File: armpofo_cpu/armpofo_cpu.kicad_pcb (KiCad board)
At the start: 2 copper layers, 82 parts, among them J1 USB_OTG, J2 Conn_01x01, J3 Conn_01x01, J4 Conn_01x16, J5 Conn_01x20, J6 Conn_02x16_Odd_Even, J7 Conn_01x08, J8 Micro_SD_Card, Q1 Q_PMOS_GDS, Q2 Q_PMOS_GDS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

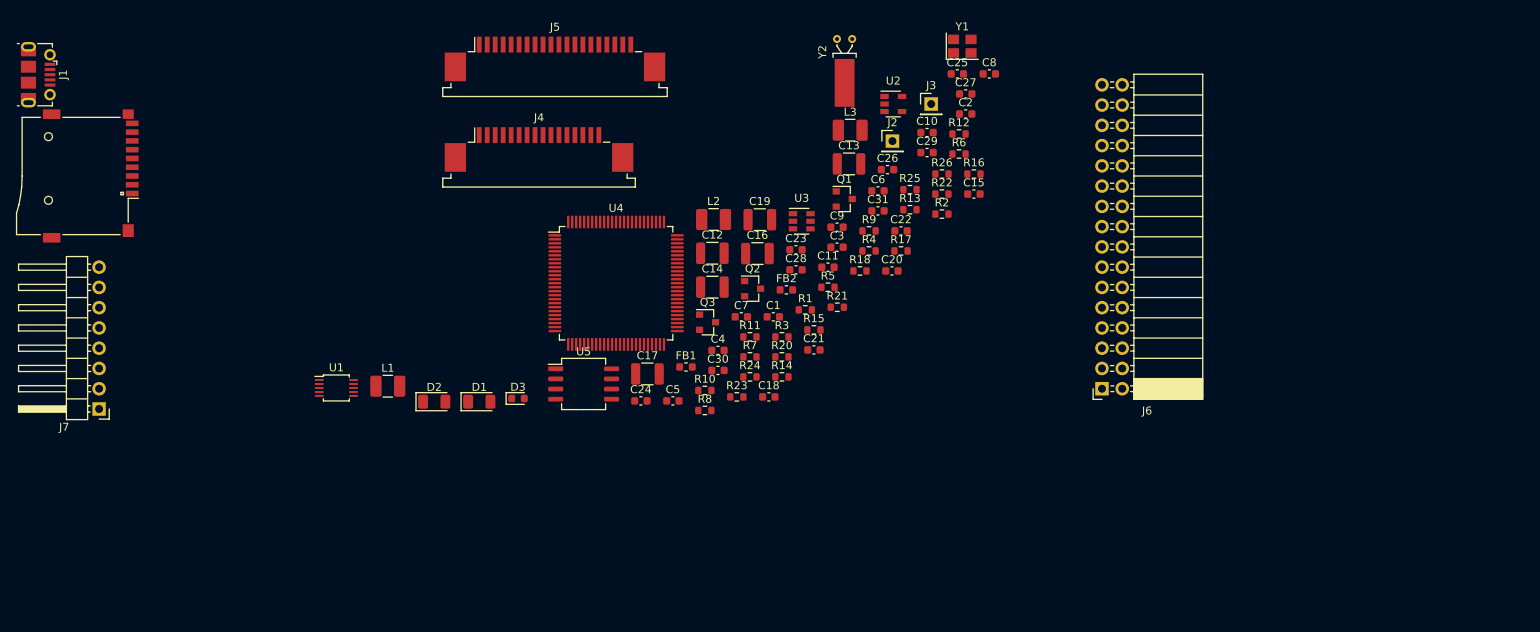
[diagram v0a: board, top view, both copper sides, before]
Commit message: - CPU board finalisch edge cuts - Keyboard mounting modified to 2.2 mm holes
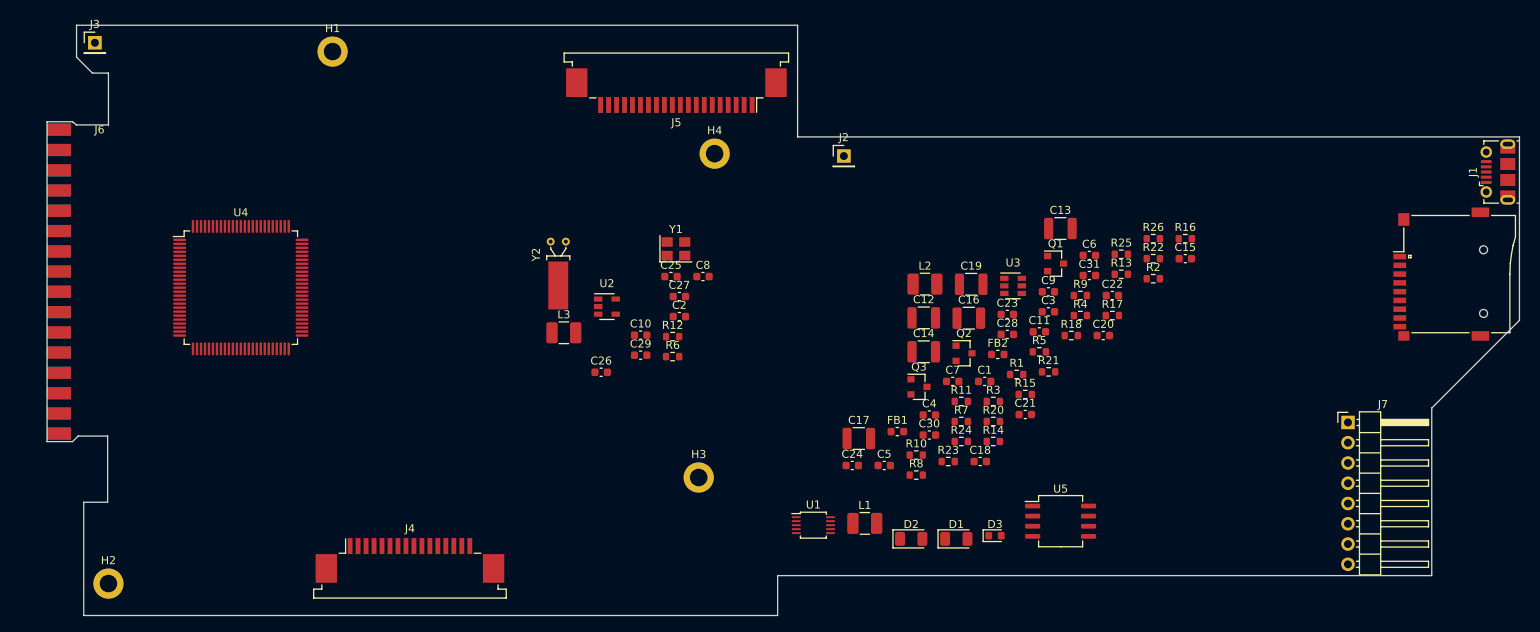
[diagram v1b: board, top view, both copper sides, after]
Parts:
- added H1: 2mm, MountingHole:MountingHole_2.2mm_M2_DIN965_Pad, F.Cu at (104.2, 73.3)
- added H2: 2mm, MountingHole:MountingHole_2.2mm_M2_DIN965_Pad, F.Cu at (76.1, 140.0)
- added H3: 2mm, MountingHole:MountingHole_2.2mm_M2_DIN965_Pad, F.Cu at (150.1, 126.7)
- added H4: 2mm, MountingHole:MountingHole_2.2mm_M2_DIN965_Pad, F.Cu at (152.1, 86.1)
- J6: footprint Connector_PinSocket_2.54mm:PinSocket_2x16_P2.54mm_Horizontal -> PROJECT_LOCAL:Conn_Edge_PinSocket_2x16_2.54mm
- moved J1 183.4 mm to (250.3, 88.4), turned to 90 degrees
- moved J8 180.3 mm to (248.5, 101.2), turned to 90 degrees
- moved J7 156.6 mm to (231.5, 119.8), turned to 0 degrees
- moved J6 134.7 mm to (69.9, 83.1), turned to 0 degrees
- moved J3 105.1 mm to (74.4, 72.2)
- moved L1 62.2 mm to (170.9, 132.5)
- moved D1 62.2 mm to (182.4, 134.4)
- moved D2 62.2 mm to (176.7, 134.4)
- moved D3 62.2 mm to (187.2, 134.0)
- moved U1 62.2 mm to (164.5, 132.7)
- moved U5 62.2 mm to (195.5, 132.2)
- moved J4 54.0 mm to (113.9, 137.1)
- moved U4 47.0 mm to (92.7, 102.9)
- moved C10 44.0 mm to (142.8, 108.9)
- moved C29 44.0 mm to (142.8, 111.4)
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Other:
- board outline added: 184.6 x 74 mm
- board text added: "Keyboard Connector"
- board text added: "LCD Connector"

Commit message: final form
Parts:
- moved J2 5.11 mm to (164.4, 89.7)
- moved J8 3.83 mm to (249.5, 104.9)
- moved J1 2.75 mm to (250.8, 91.1)
- moved J7 1.58 mm to (232.0, 121.3)
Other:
- board size 184.6 x 74 mm -> 185.1 x 74 mm

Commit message: some progress
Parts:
- added C32: 1nF, Capacitor_SMD:C_0603_1608Metric, F.Cu at (202.7, 117.8)
- added D4: SS24, Diode_SMD:D_1206_3216Metric, F.Cu at (214.4, 111.9)
- added J9: Conn_01x01, Connector_PinHeader_2.54mm:PinHeader_1x01_P2.54mm_Vertical, F.Cu at (80.7, 72.5)
- added R19: 100k, Resistor_SMD:R_0603_1608Metric, F.Cu at (145.1, 111.1)
- added R27: 100k, Resistor_SMD:R_0603_1608Metric, F.Cu at (145.1, 114.5)
- added R28: 22R, Resistor_SMD:R_0603_1608Metric, F.Cu at (245.5, 92.1)
- added R29: 22R, Resistor_SMD:R_0603_1608Metric, F.Cu at (245.5, 94.6)
- U1: footprint Package_SO:TSSOP-10_3x3mm_P0.5mm -> PROJECT_LOCAL:DLA0010A
- moved R26 110.7 mm to (96.6, 102.8)
- moved C31 106.3 mm to (92.8, 102.8)
- moved R16 103.4 mm to (112.9, 129.2)
- moved U5 102.1 mm to (96.2, 108.4)
- moved C6 95.3 mm to (105.5, 116.7)
- moved C3 89.3 mm to (104.7, 107.3)
- moved C1 82.4 mm to (104.7, 100.7)
- moved R1 79.8 mm to (114.4, 88.3)
- moved L3 78.4 mm to (211.1, 117.0)
- moved C7 76.7 mm to (105.5, 120.0)
- moved R5 76.1 mm to (119.9, 89.0)
- moved C4 74.5 mm to (105.0, 110.6)
- moved C22 71.3 mm to (130.6, 105.1)
- moved C5 69.4 mm to (105.0, 113.7)
- moved C25 66.5 mm to (208.9, 124.9)
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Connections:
- net /5V-INPUT renamed /3-5V
- J1 pad 2: /USB-DM -> Net-(J1-Pad2)
- J1 pad 3: /USB-DP -> Net-(J1-Pad3)
- U4 pad 15: /LED1 -> /ADC-5V
- U4 pad 62: Net-(U4-Pad62) -> /LED1
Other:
- board text added: "BAT+"
- board text added: "BAT-"

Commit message: routing progress 70%
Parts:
- removed C27: 100nF, Capacitor_SMD:C_0603_1608Metric
- removed R8: 0R, Resistor_SMD:R_0603_1608Metric
- added C33: 100nF, Capacitor_SMD:C_0603_1608Metric, F.Cu at (208.0, 92.0)
- added J10: Conn_01x16, Connector_PinHeader_1.27mm:PinHeader_1x16_P1.27mm_Vertical, F.Cu at (106.2, 142.9)
- added J11: Conn_01x20, Connector_PinHeader_1.27mm:PinHeader_1x20_P1.27mm_Vertical, F.Cu at (135.4, 71.1)
- J4: moved to B.Cu
- R10: footprint Resistor_SMD:R_0603_1608Metric -> Resistor_SMD:R_1206_3216Metric
- R4: value 0R -> 1k
- U1: value TPS63802 -> TPS63030DSK; footprint PROJECT_LOCAL:DLA0010A -> Package_SON:WSON-10-1EP_2.5x2.5mm_P0.5mm_EP1.2x2mm
- moved R4 69.3 mm to (149.4, 103.1), turned to 180 degrees
- moved C32 58.3 mm to (146.3, 103.1), turned to 180 degrees
- moved C25 45.6 mm to (176.5, 92.8), turned to 270 degrees
- moved U3 44.6 mm to (171.8, 91.8), turned to 180 degrees
- moved L3 43.7 mm to (178.0, 88.5), turned to 180 degrees
- moved C24 41.2 mm to (167.8, 95.2), turned to 180 degrees
- moved R10 41.1 mm to (171.8, 88.2)
- moved D4 39.9 mm to (179.2, 93.0), turned to 270 degrees
- moved R5 38.6 mm to (136.4, 124.0), turned to 270 degrees
- moved R1 38.6 mm to (146.8, 109.2)
- moved C10 38.6 mm to (143.5, 109.2), turned to 180 degrees
- moved R12 31.7 mm to (167.0, 92.8), turned to 270 degrees
- moved Q1 28.8 mm to (182.8, 91.0), turned to 270 degrees
- moved R11 28.3 mm to (168.8, 92.8), turned to 90 degrees
- moved C1 27.6 mm to (129.3, 113.2)
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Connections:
- net Net-(J5-Pad12) renamed /LCD-CTRPWM
- C32 pad 1: Net-(C25-Pad1) -> /I-CHARGE
- C32 pad 2: /BAT+ -> GND
- D3 pad 1: /LED1 -> Net-(D3-Pad1)
- D3 pad 2: Net-(D3-Pad2) -> +3V3
- H1 pad 1: Earth_Protective -> Net-(H1-Pad1)
- H2 pad 1: Earth_Protective -> Net-(H2-Pad1)
- H3 pad 1: Earth_Protective -> Net-(H3-Pad1)
- H4 pad 1: Earth_Protective -> Net-(H4-Pad1)
- R25 pad 1: Net-(D3-Pad2) -> /LED1
- R25 pad 2: +3V3 -> Net-(D3-Pad1)
- R4 pad 1: /3-5V -> Net-(R4-Pad1)
- R4 pad 2: Net-(R4-Pad2) -> /I-CHARGE
- U1 pad 1: /3-5V -> /5VINT
- U1 pad 10: /3-5V -> Net-(R3-Pad2)
- U1 pad 2: Net-(R4-Pad2) -> Net-(L1-Pad2)
- U1 pad 4: Net-(R3-Pad2) -> Net-(L1-Pad1)
- U1 pad 5: Net-(U1-Pad5) -> /3-5V
- U1 pad 6: /5VINT -> Net-(C33-Pad1)
- U1 pad 7: Net-(L1-Pad2) -> Net-(C33-Pad1)
- U1 pad 8: GND -> Net-(C33-Pad1)
- U1 pad 9: Net-(L1-Pad1) -> GND
- U3 pad 1: /I-CHARGE -> Net-(R4-Pad1)
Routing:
- net +3V3: track 0.00 -> 240.6 mm, vias 0 -> 22
- net /BOOT0: track 0.00 -> 125.4 mm, vias 0 -> 2
- net GND: track 0.00 -> 112.4 mm, vias 0 -> 43
- net /USB5V: track 0.00 -> 108.0 mm
- net /5VINT: track 0.00 -> 107.0 mm, vias 0 -> 5
- net /TRACE-RX: track 0.00 -> 98.7 mm
- net /TRACE-TX: track 0.00 -> 98.5 mm
- net /SWDIO: track 0.00 -> 98.4 mm
- net /RESET: track 0.00 -> 95.8 mm
- net /CHARGE-PWM: track 0.00 -> 86.6 mm, vias 0 -> 2
- net /SDCARD-D2: track 0.00 -> 84.1 mm
- net /SDCARD-D3: track 0.00 -> 84.1 mm
- net /SOUND-LATCH: track 0.00 -> 83.9 mm, vias 0 -> 4
- net /SWDC: track 0.00 -> 82.7 mm
- net /SDCARD-CMD: track 0.00 -> 81.4 mm
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- added copper zone on F.Cu, net /3-5V
- added copper zone on F.Cu, net /5VINT
- added copper zone on B.Cu, net GND
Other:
- net class Default: trace_width 0.25 -> 0.2; via_dia 0.8 -> 0.6; via_drill 0.4 -> 0.3
- rule trace_min: 0.2 -> 0.156
- rule via_min_size: 0.4 -> 0.6
- board text added: "1"
- board text added: "16"
- board text added: "20"
- board text added: "5V"
- board text added: "GND"

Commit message: routing finished.
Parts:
- moved R5 18.3 mm to (119.7, 131.5), turned to 90 degrees
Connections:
- J6 pad 10: /PB6 -> /PA2
- J6 pad 11: /PA2 -> /PA5
- J6 pad 12: /PB7 -> /PA4
- J6 pad 13: /PA3 -> /PA7
- J6 pad 14: /PB11 -> /PA6
- J6 pad 15: /PA4 -> /PB5
- J6 pad 16: /PB12 -> /PA8
- J6 pad 17: /PA5 -> /PB7
- J6 pad 18: /PB13 -> /PB6
- J6 pad 19: /PA6 -> /PB12
- J6 pad 20: /PB14 -> /PB11
- J6 pad 21: /PA7 -> /PB14
- J6 pad 22: /PB15 -> /PB13
- J6 pad 23: /PA8 -> /PC1
- J6 pad 24: /PC1 -> /PB15
- J6 pad 25: /PD0 -> /PC5
- J6 pad 28: /PC5 -> /PD0
- J6 pad 7: /PA0 -> /PA1
- J6 pad 8: /PB5 -> /PA0
- J6 pad 9: /PA1 -> /PA3
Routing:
- net +3V3: track 240.6 -> 433.5 mm, vias 22 -> 29
- net /USB-DM: track 22.6 -> 152.7 mm, vias 2 -> 4
- net /USB-DP: track 24.8 -> 154.0 mm, vias 2 -> 4
- net /5VINT: track 107.0 -> 183.9 mm, vias 5 -> 10
- net /LED1: track 70.1 -> 136.5 mm, vias 0 -> 4
- net /SDCARD-D2: track 84.1 -> 149.3 mm, vias 0 -> 4
- net /SDCARD-D1: track 75.5 -> 139.1 mm, vias 0 -> 4
- net /SDCARD-D3: track 84.1 -> 145.4 mm, vias 0 -> 4
- net /SDCARD-D0: track 80.4 -> 139.6 mm, vias 0 -> 4
- net /SDCARD-CK: track 80.7 -> 139.0 mm, vias 0 -> 2
- net /PA0: track 13.0 -> 69.5 mm, vias 0 -> 5
- net /SDCARD-CMD: track 81.4 -> 137.6 mm, vias 0 -> 2
- net /PA1: track 13.0 -> 66.2 mm, vias 0 -> 4
- net /PA2: track 12.9 -> 65.1 mm, vias 0 -> 5
- net /PA3: track 12.7 -> 61.9 mm, vias 0 -> 4
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
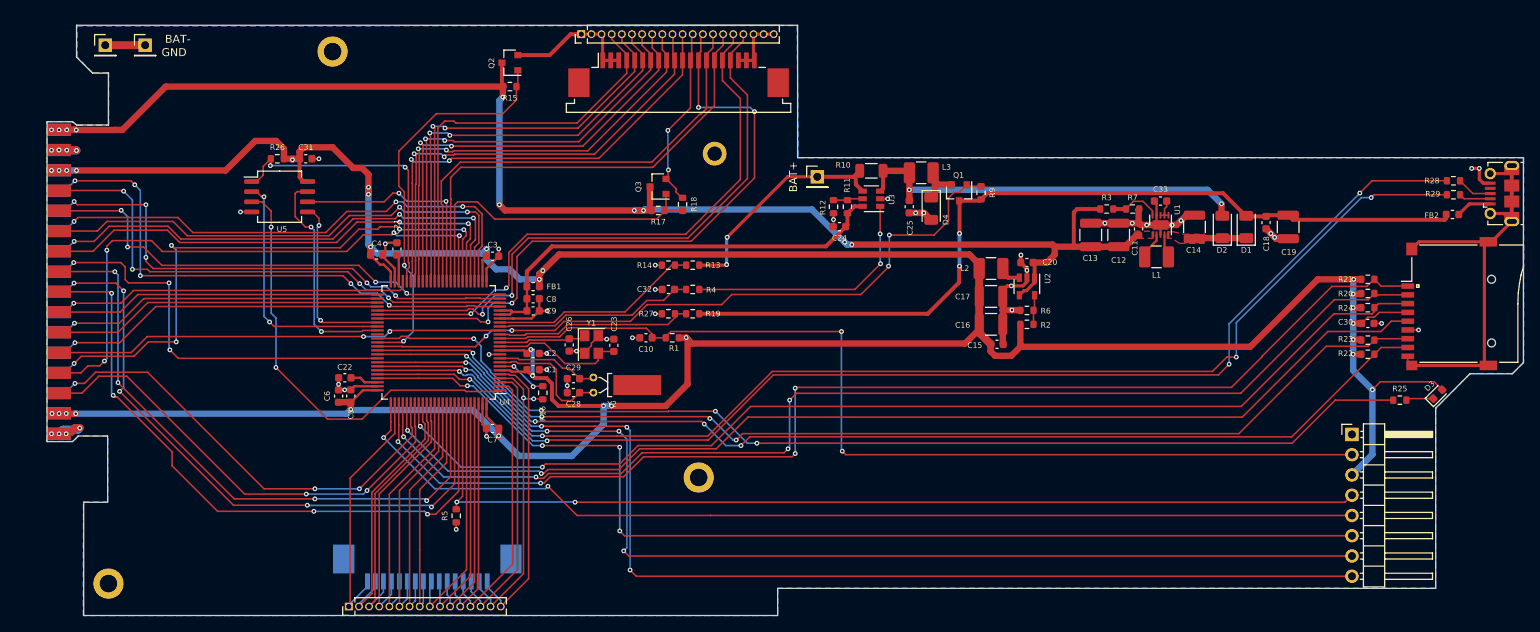
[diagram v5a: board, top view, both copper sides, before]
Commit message: PCB corrections some items moved to the backside
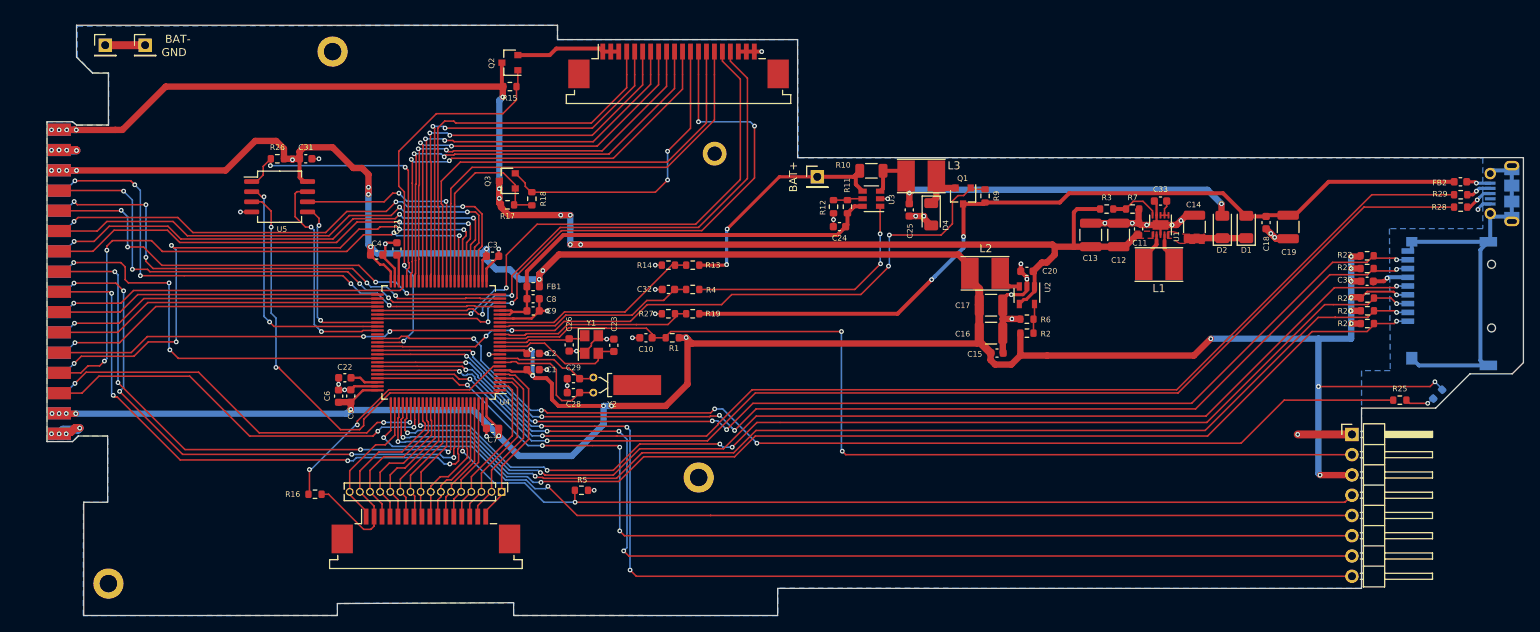
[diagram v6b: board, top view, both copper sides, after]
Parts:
- removed J11: Conn_01x20, Connector_PinHeader_1.27mm:PinHeader_1x20_P1.27mm_Vertical
- D3, J1, J8: moved to B.Cu
- J4: moved to F.Cu
- L1, L2, L3: footprint Inductor_SMD:L_1210_3225Metric_Pad1.42x2.65mm_HandSolder -> Inductor_SMD:L_Taiyo-Yuden_NR-40xx_HandSoldering
- moved R16 31.3 mm to (102.0, 128.8), turned to 180 degrees
- moved J10 24.0 mm to (125.4, 128.5), turned to 270 degrees
- moved R18 18.9 mm to (129.2, 91.8)
- moved Q3 18.9 mm to (126.1, 89.5)
- moved R17 18.9 mm to (126.1, 92.5)
- moved R5 16.0 mm to (135.4, 128.3), turned to 180 degrees
- moved R22 12.4 mm to (233.9, 98.9)
- moved R23 8.97 mm to (233.9, 100.5)
- moved R21 5.55 mm to (233.9, 107.4)
- moved C30 5.28 mm to (233.9, 102.1)
- moved J4 4.53 mm to (115.9, 133.4)
- moved FB2 4.22 mm to (245.6, 89.6)
- moved R28 3.42 mm to (245.6, 92.8)
- moved R20 2.17 mm to (233.9, 105.8)
- moved R24 1.21 mm to (233.9, 104.2)
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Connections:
- J4 pad 1: /KEY-R1 -> /KEY-C8
- J4 pad 10: /KEY-C2 -> /KEY-R7
- J4 pad 11: /KEY-C3 -> /KEY-R6
- J4 pad 12: /KEY-C4 -> /KEY-R5
- J4 pad 13: /KEY-C5 -> /KEY-R4
- J4 pad 14: /KEY-C6 -> /KEY-R3
- J4 pad 15: /KEY-C7 -> /KEY-R2
- J4 pad 16: /KEY-C8 -> /KEY-R1
- J4 pad 2: /KEY-R2 -> /KEY-C7
- J4 pad 3: /KEY-R3 -> /KEY-C6
- J4 pad 4: /KEY-R4 -> /KEY-C5
- J4 pad 5: /KEY-R5 -> /KEY-C4
- J4 pad 6: /KEY-R6 -> /KEY-C3
- J4 pad 7: /KEY-R7 -> /KEY-C2
- J4 pad 8: /KEY-R8 -> /KEY-C1
- J4 pad 9: /KEY-C1 -> /KEY-R8
- U4 pad 2: /KEY-C5 -> /KEY-R4
- U4 pad 3: /KEY-C6 -> /KEY-R3
- U4 pad 4: /KEY-C7 -> /KEY-R2
- U4 pad 5: /KEY-C8 -> /KEY-R1
- U4 pad 77: /KEY-R1 -> /KEY-C8
- U4 pad 84: /KEY-R2 -> /KEY-C7
- U4 pad 85: /KEY-R3 -> /KEY-C6
- U4 pad 86: /KEY-R4 -> /KEY-C5
- U4 pad 87: /KEY-R5 -> /KEY-C4
- U4 pad 88: /KEY-R6 -> /KEY-C3
- U4 pad 89: /KEY-R7 -> /KEY-C2
- U4 pad 90: /KEY-R8 -> /KEY-C1
- U4 pad 95: /KEY-C1 -> /KEY-R8
- U4 pad 96: /KEY-C2 -> /KEY-R7
- U4 pad 97: /KEY-C3 -> /KEY-R6
- U4 pad 98: /KEY-C4 -> /KEY-R5
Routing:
- net /WAKEUP: track 6.54 -> 32.7 mm
- net /KEY-C8: track 37.0 -> 18.1 mm
- net /LCD-CON-PWM: track 41.8 -> 25.2 mm
- net /KEY-C5: track 34.6 -> 18.4 mm
- net /KEY-C6: track 35.5 -> 19.4 mm
- net /KEY-R5: track 31.5 -> 15.4 mm
- net /LCD-CTRPWM: track 22.7 -> 38.4 mm
- net /KEY-R6: track 31.0 -> 15.7 mm
- net /KEY-C1: track 30.6 -> 15.6 mm
- net /KEY-R7: track 30.6 -> 16.2 mm
- net /KEY-C2: track 30.2 -> 16.1 mm
- net /KEY-C3: track 30.0 -> 16.4 mm
- net /KEY-R8: track 30.2 -> 16.7 mm
- net /KEY-C4: track 29.8 -> 17.5 mm
- net /KEY-R4: track 32.0 -> 20.2 mm
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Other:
- outline, holes or cut-outs redrawn
- board text added: "C8"
- board text added: "R1"

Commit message: finalizing sizes, positions
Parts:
- added J11: Conn_01x20, Connector_FFC-FPC:TE_2-84952-0_1x20-1MP_P1.0mm_Horizontal, B.Cu at (147.6, 79.1)
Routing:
- net /LCD-5V: track 13.1 -> 36.0 mm, vias 0 -> 3
- net /LCD-D3: track 53.4 -> 58.7 mm, vias 2 -> 3
- net /LCD-D4: track 54.9 -> 60.1 mm, vias 2 -> 3
- net /LCD-D5: track 55.7 -> 60.9 mm, vias 2 -> 3
- net /LCD-D2: track 52.3 -> 57.4 mm, vias 2 -> 3
- net /LCD-D7: track 58.0 -> 63.1 mm, vias 2 -> 3
- net /LCD-D6: track 57.1 -> 62.2 mm, vias 2 -> 3
- net /LCD-D1: track 51.4 -> 56.4 mm, vias 2 -> 3
- net /LCD-D0: track 49.8 -> 54.4 mm, vias 0 -> 1
- net /LCD-RS: track 57.8 -> 60.7 mm, vias 0 -> 1
- net /LCD-E: track 56.8 -> 59.6 mm, vias 0 -> 1
- net GND: track 124.1 -> 126.7 mm
- net /LCD-R~W: track 72.5 -> 75.0 mm, vias 2 -> 3
- net /LCD-CS: track 72.1 -> 74.5 mm, vias 2 -> 3
- net /LCD-CTRPWM: track 38.4 -> 40.8 mm, vias 2 -> 3
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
